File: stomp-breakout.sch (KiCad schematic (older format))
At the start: 9 parts, among them J1 Stomp_Connector, J2 JO, J3 JI, J4 Power_SIDE, J5 Power_TOP

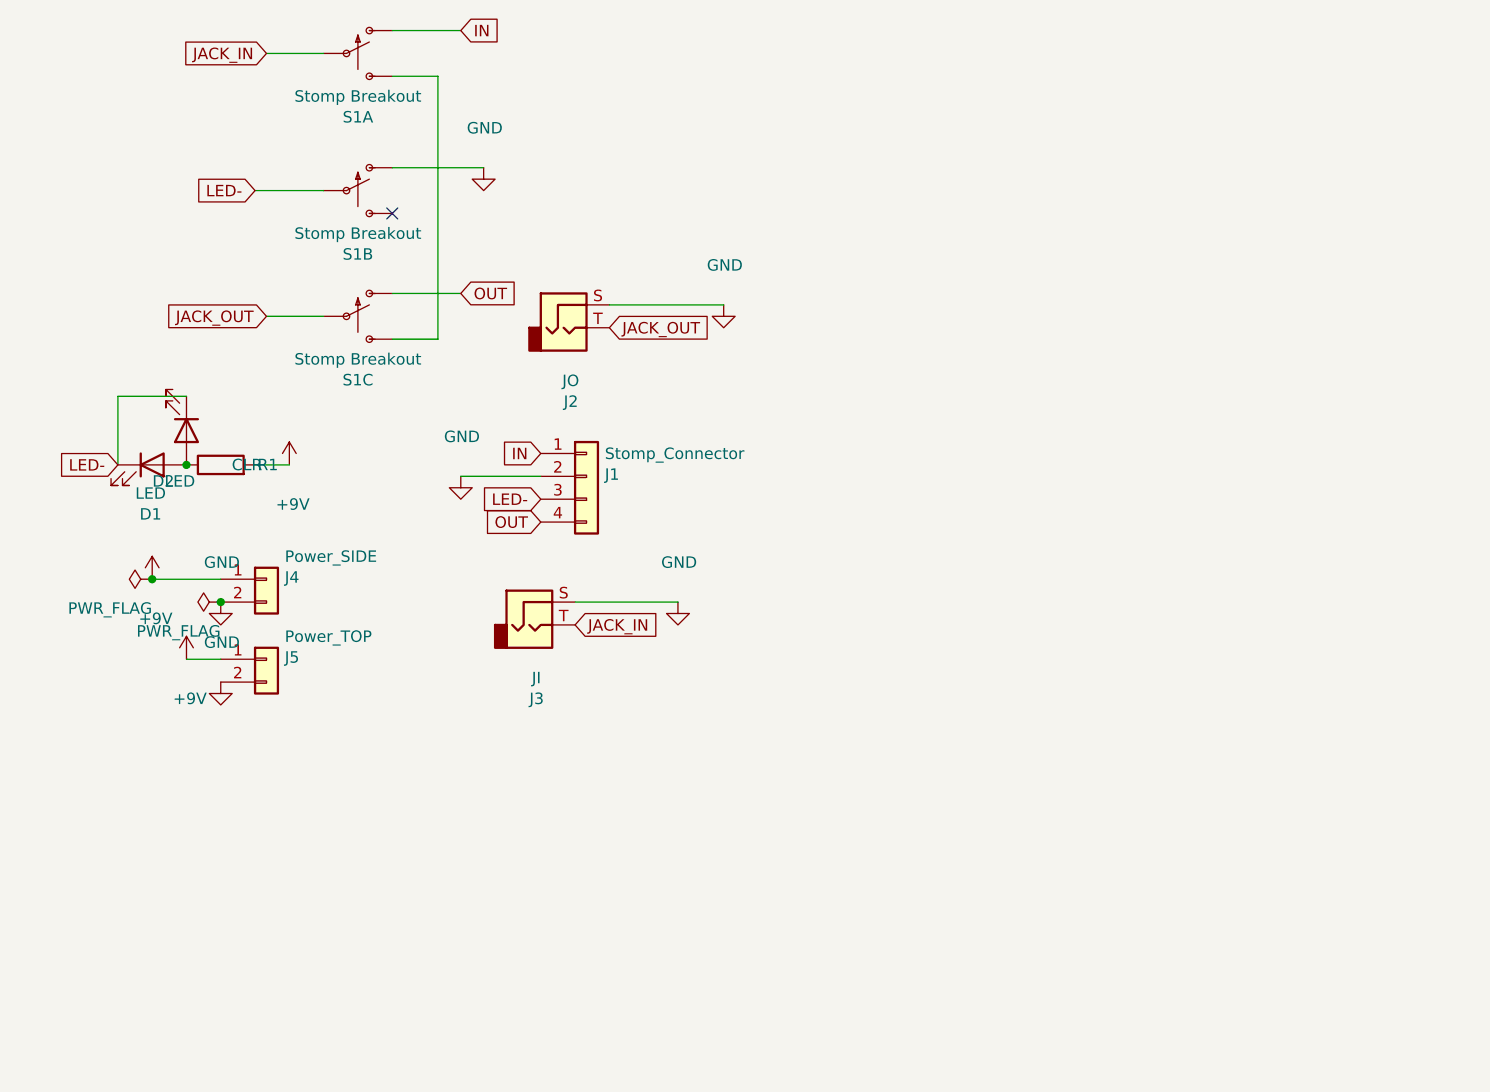
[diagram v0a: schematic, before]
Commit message: v0.2: board input grounded in bypass
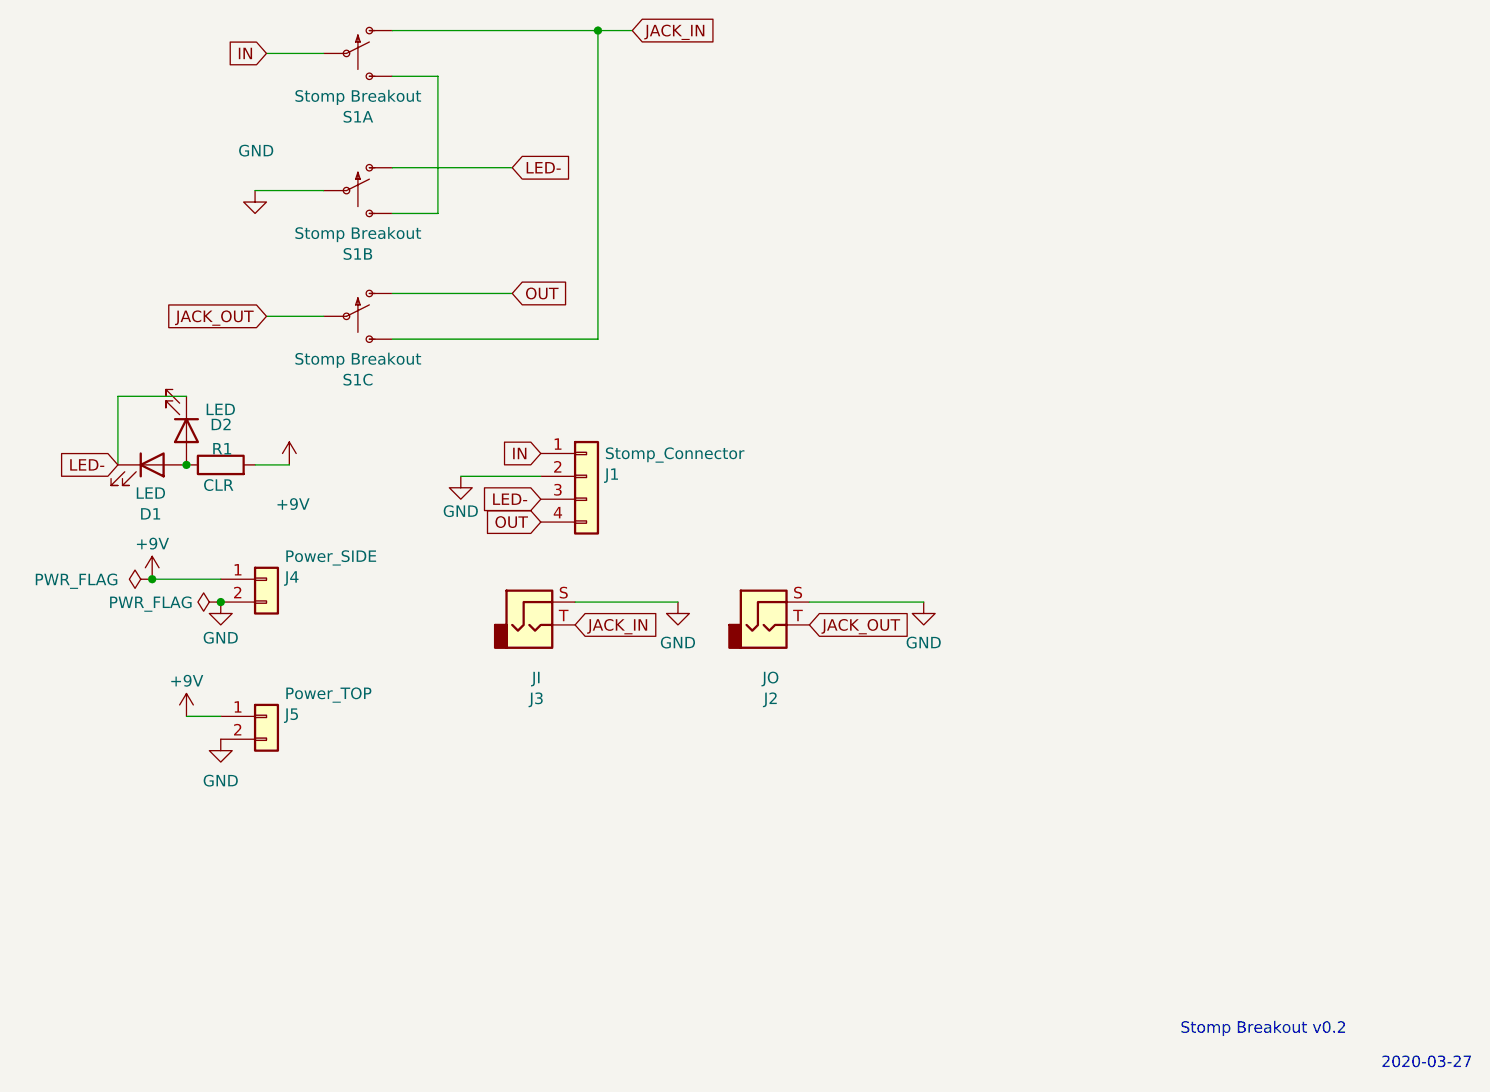
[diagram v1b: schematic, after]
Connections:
- net GND: now also S1.5 (P); no longer S1.4 (O)
- net IN: now also S1.2 (P); no longer S1.1 (O)
- net JACK_IN: now also S1.1 (O), S1.9 (S); no longer S1.2 (P)
- net LED-: now also S1.4 (O); no longer S1.5 (P)
- net at S1.3 (S): now also S1.6 (S); no longer S1.9 (S)
- no-connect marks 1 -> 0
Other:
- note added: "2020-03-27"
- note added: "Stomp Breakout v0.2"
- moved on the sheet: J2, J5
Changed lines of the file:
@@
 EESchema Schematic File Version 5
-EELAYER 32 0
+EELAYER 33 0
 EELAYER END
 $Descr A4 11693 8268
@@
 Connection ~ 2950 5500
 Connection ~ 3250 5600
-NoConn ~ 4000 3900
+Connection ~ 4900 3100
 Wire Wire Line
 	2800 4700 2800 5000
@@
 	3100 4700 2800 4700
 Wire Wire Line
-	3100 5850 3250 5850
+	3100 6100 3250 6100
 Wire Wire Line
 	3400 3800 3700 3800
@@
 	3450 4350 3700 4350
 Wire Wire Line
-	4000 3100 4300 3100
+	4000 3100 4900 3100
 Wire Wire Line
 	4000 3300 4200 3300
 Wire Wire Line
-	4000 3700 4400 3700
-Wire Wire Line
-	4000 4250 4300 4250
-Wire Wire Line
-	4200 3300 4200 4450
-Wire Wire Line
-	4200 4450 4000 4450
+	4000 3700 4525 3700
+Wire Wire Line
+	4000 3900 4200 3900
+Wire Wire Line
+	4000 4250 4525 4250
+Wire Wire Line
+	4200 3900 4200 3300
 Wire Wire Line
 	4300 5050 4650 5050
@@
 	4800 5600 5250 5600
 Wire Wire Line
-	5450 4300 4950 4300
+	4900 3100 4900 4450
+Wire Wire Line
+	4900 3100 5050 3100
+Wire Wire Line
+	4900 4450 4000 4450
+Wire Wire Line
+	6325 5600 5825 5600
+Text Notes 8175 7500 2    50   ~ 0
+Stomp Breakout v0.2
+Text Notes 8725 7650 2    50   ~ 0
+2020-03-27
 Text GLabel 2800 5000 0    50   Input ~ 0
 LED-
-Text GLabel 3400 3800 0    50   Input ~ 0
-LED-
 Text GLabel 3450 3200 0    50   Input ~ 0
-JACK_IN
+IN
 Text GLabel 3450 4350 0    50   Input ~ 0
 JACK_OUT
-Text GLabel 4300 3100 2    50   Input ~ 0
-IN
-Text GLabel 4300 4250 2    50   Input ~ 0
+Text GLabel 4525 3700 2    50   Input ~ 0
+LED-
+Text GLabel 4525 4250 2    50   Input ~ 0
 OUT
 Text GLabel 4650 4950 0    50   Input ~ 0
@@
 Text GLabel 4800 5700 2    50   Input ~ 0
 JACK_IN
-Text GLabel 4950 4400 2    50   Input ~ 0
+Text GLabel 5050 3100 2    50   Input ~ 0
+JACK_IN
+Text GLabel 5825 5700 2    50   Input ~ 0
 JACK_OUT
 $Comp
@@
 P 2950 5500
 F 0 "#FLG0101" H 2950 5575 50  0001 C CNN
-F 1 "PWR_FLAG" V 2822 5500 50  0000 L CNN
+F 1 "PWR_FLAG" V 2947 5647 50  0000 L CNN
 F 2 "" H 2950 5500 50  0001 C CNN
 F 3 "~" H 2950 5500 50  0001 C CNN
@@
 P 3250 5600
 F 0 "#FLG0102" H 3250 5675 50  0001 C CNN
-F 1 "PWR_FLAG" V 3122 5600 50  0000 L CNN
+F 1 "PWR_FLAG" V 3247 5722 50  0000 L CNN
 F 2 "" H 3250 5600 50  0001 C CNN
 F 3 "~" H 3250 5600 50  0001 C CNN
@@
 P 2950 5500
 F 0 "#PWR0108" H 2950 5350 50  0001 C CNN
-F 1 "+9V" H 2965 5327 50  0000 C CNN
+F 1 "+9V" H 2950 5654 50  0000 C CNN
 F 2 "" H 2950 5500 50  0001 C CNN
 F 3 "" H 2950 5500 50  0001 C CNN
@@
 L power:+9V #PWR0105
 U 1 1 5E7A772B
-P 3100 5850
-F 0 "#PWR0105" H 3100 5700 50  0001 C CNN
-F 1 "+9V" H 3115 5677 50  0000 C CNN
-F 2 "" H 3100 5850 50  0001 C CNN
-F 3 "" H 3100 5850 50  0001 C CNN
-	1    3100 5850
+P 3100 6100
+F 0 "#PWR0105" H 3100 5950 50  0001 C CNN
+F 1 "+9V" H 3100 6254 50  0000 C CNN
+F 2 "" H 3100 6100 50  0001 C CNN
+F 3 "" H 3100 6100 50  0001 C CNN
+	1    3100 6100
 	1    0    0    -1
 $EndComp
@@
 P 3250 5600
 F 0 "#PWR0107" H 3250 5350 50  0001 C CNN
-F 1 "GND" H 3255 5773 50  0000 C CNN
+F 1 "GND" H 3250 5442 50  0000 C CNN
 F 2 "" H 3250 5600 50  0001 C CNN
 F 3 "" H 3250 5600 50  0001 C CNN
@@
 L power:GND #PWR0106
 U 1 1 5E7A8D18
-P 3250 5950
-F 0 "#PWR0106" H 3250 5700 50  0001 C CNN
-F 1 "GND" H 3255 6123 50  0000 C CNN
-F 2 "" H 3250 5950 50  0001 C CNN
-F 3 "" H 3250 5950 50  0001 C CNN
-	1    3250 5950
+P 3250 6200
+F 0 "#PWR0106" H 3250 5950 50  0001 C CNN
+F 1 "GND" H 3250 6017 50  0000 C CNN
+F 2 "" H 3250 6200 50  0001 C CNN
+F 3 "" H 3250 6200 50  0001 C CNN
+	1    3250 6200
+	1    0    0    -1
+$EndComp
+$Comp
+L power:GND #PWR0101
+U 1 1 5E7AA0AF
+P 3400 3800
+F 0 "#PWR0101" H 3400 3550 50  0001 C CNN
+F 1 "GND" H 3405 3973 50  0000 C CNN
+F 2 "" H 3400 3800 50  0001 C CNN
+F 3 "" H 3400 3800 50  0001 C CNN
+	1    3400 3800
 	1    0    0    -1
 $EndComp
@@
 P 4300 5050
 F 0 "#PWR0103" H 4300 4800 50  0001 C CNN
-F 1 "GND" H 4305 5223 50  0000 C CNN
+F 1 "GND" H 4300 4896 50  0000 C CNN
 F 2 "" H 4300 5050 50  0001 C CNN
 F 3 "" H 4300 5050 50  0001 C CNN
 	1    4300 5050
-	1    0    0    -1
-$EndComp
-$Comp
-L power:GND #PWR0101
-U 1 1 5E7AA0AF
-P 4400 3700
-F 0 "#PWR0101" H 4400 3450 50  0001 C CNN
-F 1 "GND" H 4405 3873 50  0000 C CNN
-F 2 "" H 4400 3700 50  0001 C CNN
-F 3 "" H 4400 3700 50  0001 C CNN
-	1    4400 3700
 	1    0    0    -1
 $EndComp
@@
 P 5250 5600
 F 0 "#PWR0102" H 5250 5350 50  0001 C CNN
-F 1 "GND" H 5255 5773 50  0000 C CNN
+F 1 "GND" H 5250 5421 50  0000 C CNN
 F 2 "" H 5250 5600 50  0001 C CNN
 F 3 "" H 5250 5600 50  0001 C CNN
@@
 L power:GND #PWR0104
 U 1 1 5E7C1C22
-P 5450 4300
-F 0 "#PWR0104" H 5450 4050 50  0001 C CNN
-F 1 "GND" H 5455 4473 50  0000 C CNN
-F 2 "" H 5450 4300 50  0001 C CNN
-F 3 "" H 5450 4300 50  0001 C CNN
-	1    5450 4300
+P 6325 5600
+F 0 "#PWR0104" H 6325 5350 50  0001 C CNN
+F 1 "GND" H 6325 5421 50  0000 C CNN
+F 2 "" H 6325 5600 50  0001 C CNN
+F 3 "" H 6325 5600 50  0001 C CNN
+	1    6325 5600
 	1    0    0    -1
 $EndComp
@@
 U 1 1 5E759C2C
 P 3250 5000
-F 0 "R1" V 3250 4794 50  0000 C CNN
-F 1 "CLR" V 3250 4885 50  0000 C CNN
+F 0 "R1" V 3319 4994 50  0000 C CNN
+F 1 "CLR" V 3160 5010 50  0000 C CNN
 F 2 "rockola_kicad_footprints:Resistor_0.25W_Standing" V 3180 5000 50  0001 C CNN
 F 3 "~" H 3250 5000 50  0001 C CNN
@@
 U 1 1 5E795386
 P 3100 4850
-F 0 "D2" V 3322 4797 50  0000 R CNN
-F 1 "LED" V 3322 4888 50  0000 R CNN
+F 0 "D2" V 3075 5050 50  0000 R CNN
+F 1 "LED" V 3009 5066 50  0000 R CNN
 F 2 "LED_THT:LED_D3.0mm" H 3100 4850 50  0001 C CNN
 F 3 "~" H 3100 4850 50  0001 C CNN
@@
 L rockola_kicad_symbols:Power_Connector J5
 U 1 1 5E771978
-P 3450 5850
-F 0 "J5" H 3530 5858 50  0000 L CNN
-F 1 "Power_TOP" H 3530 5949 50  0000 L CNN
-F 2 "rockola_kicad_footprints:Power_Header_2pin_TOP_ALT" H 3450 5850 50  0001 C CNN
-F 3 "~" H 3450 5850 50  0001 C CNN
-	1    3450 5850
+P 3450 6100
+F 0 "J5" H 3530 6108 50  0000 L CNN
+F 1 "Power_TOP" H 3530 6199 50  0000 L CNN
+F 2 "rockola_kicad_footprints:Power_Header_2pin_TOP_ALT" H 3450 6100 50  0001 C CNN
+F 3 "~" H 3450 6100 50  0001 C CNN
+	1    3450 6100
 	1    0    0    -1
 $EndComp
@@
 L Connector:AudioJack2 J2
 U 1 1 5E74EECC
-P 4750 4400
-F 0 "J2" H 4782 4077 50  0000 C CNN
-F 1 "JO" H 4781 4168 50  0000 C CNN
-F 2 "rockola_kicad_footprints:2PADS_TS_Horizontal" H 4750 4400 50  0001 C CNN
-F 3 "~" H 4750 4400 50  0001 C CNN
-	1    4750 4400
-	1    0    0    -1
-$EndComp
+P 5625 5700
+F 0 "J2" H 5657 5377 50  0000 C CNN
+F 1 "JO" H 5656 5468 50  0000 C CNN
+F 2 "rockola_kicad_footprints:2PADS_TS_Horizontal" H 5625 5700 50  0001 C CNN
+F 3 "~" H 5625 5700 50  0001 C CNN
+	1    5625 5700
+	1    0    0    -1
+$EndComp
